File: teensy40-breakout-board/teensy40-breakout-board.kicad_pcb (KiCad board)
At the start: 2 copper layers, 18 x 56.1 mm, 3 parts, among them J1 Conn_01x08, J2 Conn_01x08, U1 Teensy4.0_WithBottomAndEdge

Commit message: Complete routing
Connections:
- net Net-(J1-Pad6) renamed VCC
- net Net-(J1-Pad7) renamed +3V3
- net Net-(J1-Pad8) renamed GND
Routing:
- net Net-(J2-Pad5): track 0.00 -> 28.3 mm, vias 0 -> 1
- net Net-(J2-Pad4): track 0.00 -> 23.4 mm, vias 0 -> 1
- net +3V3: track 0.00 -> 21.2 mm
- net Net-(J2-Pad7): track 0.00 -> 19.9 mm
- net VCC: track 0.00 -> 17.0 mm
- net Net-(J2-Pad6): track 0.00 -> 16.3 mm
- net Net-(J2-Pad3): track 19.9 -> 18.4 mm
- net Net-(J1-Pad5): track 26.1 -> 24.7 mm
- added copper zone on B.Cu, net GND
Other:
- net class Default: clearance 0.2 -> 0.254; trace_width 0.25 -> 0.254; via_dia 0.8 -> 0.762; via_drill 0.4 -> 0.381
- net class Power added: clearance 0.254, trace_width 1.27, via_dia 1.524, via_drill 0.762
- rule trace_clearance: 0.2 -> 0.254

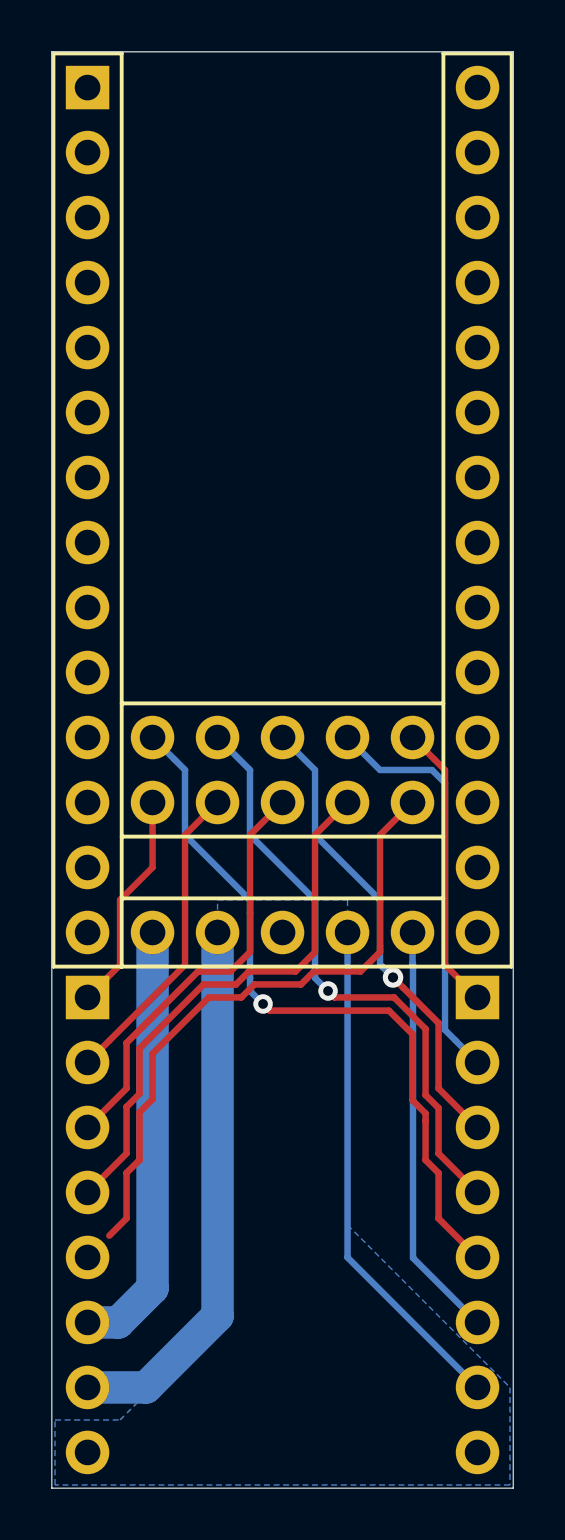
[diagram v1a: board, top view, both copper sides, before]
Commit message: Add top silkscreen labels
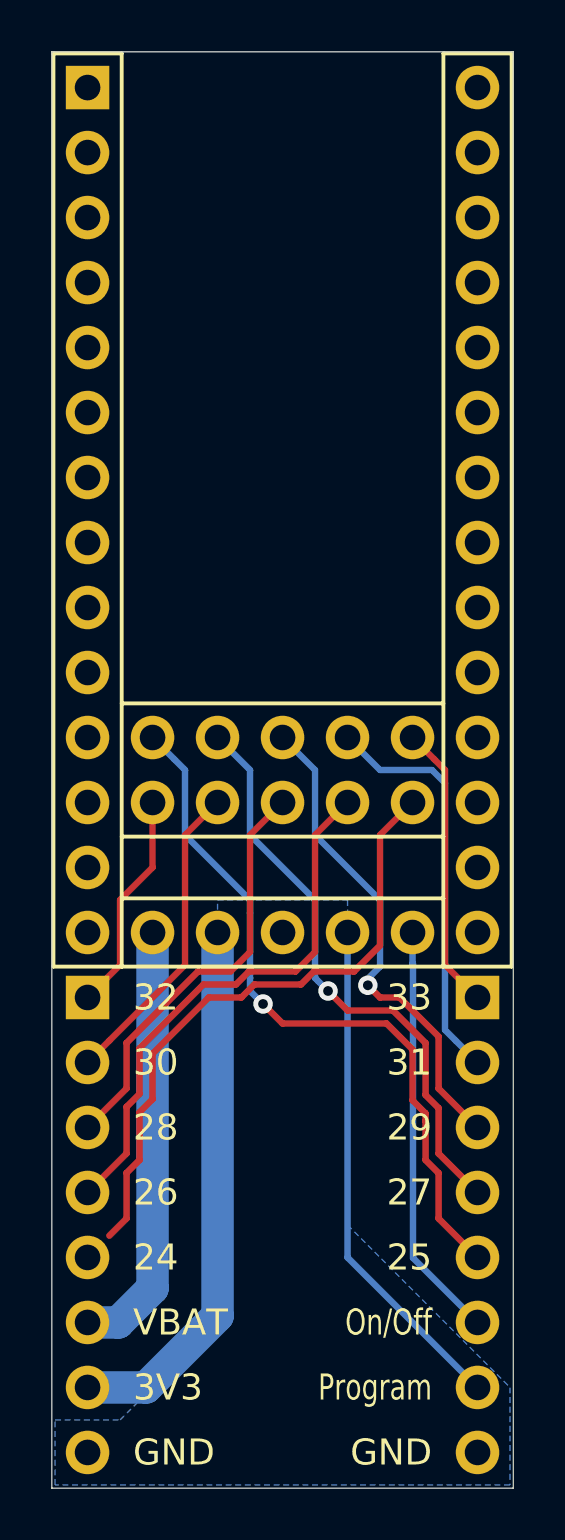
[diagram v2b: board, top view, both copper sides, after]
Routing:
- net Net-(J2-Pad3): track 18.4 -> 19.3 mm
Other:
- board text added: "24"
- board text added: "25"
- board text added: "26"
- board text added: "27"
- board text added: "28"
- board text added: "29"
- board text added: "30"
- board text added: "31"
- board text added: "32"
- board text added: "33"
- board text added: "3V3"
- board text added: "GND"
- board text added: "On/Off"
- board text added: "Program"
- board text added: "VBAT"

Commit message: Label all breakout pins
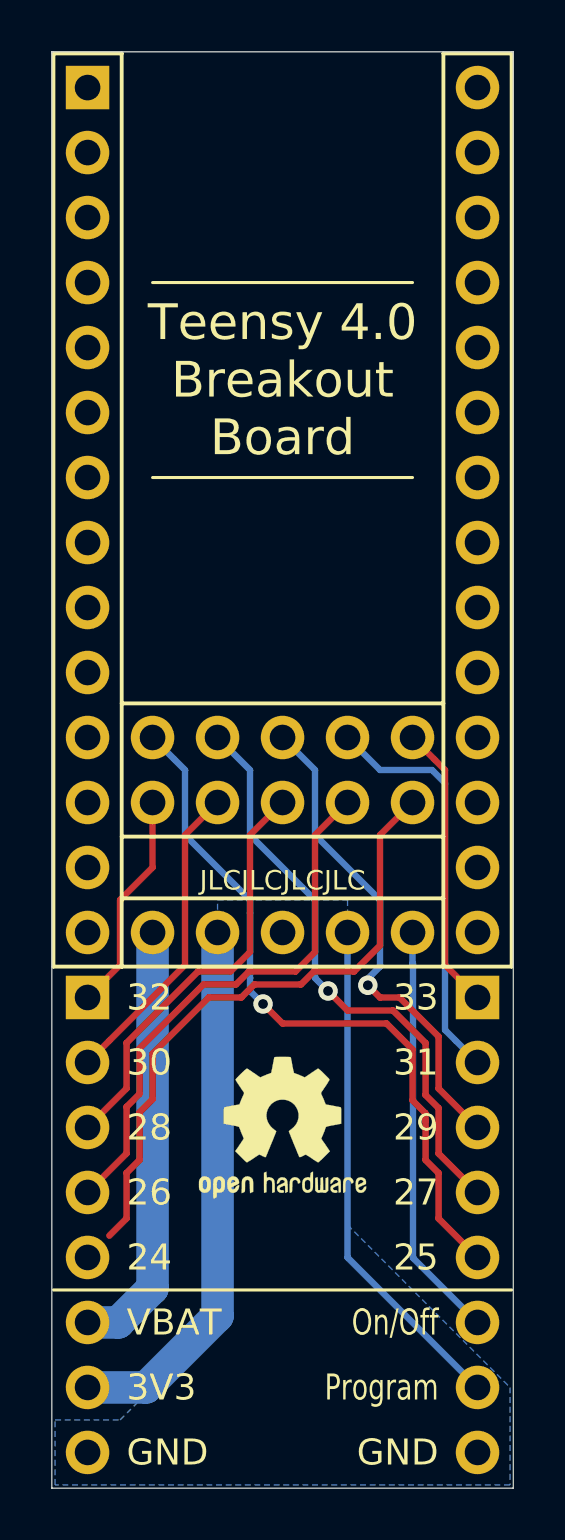
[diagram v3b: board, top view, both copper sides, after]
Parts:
- added REF**: OSHW-Logo2_7.3x6mm_SilkScreen, Symbol:OSHW-Logo2_7.3x6mm_SilkScreen, F.Cu at (134.6, 116.8)
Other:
- board text added: "0"
- board text added: "1"
- board text added: "10"
- board text added: "11"
- board text added: "12"
- board text added: "13"
- board text added: "14"
- board text added: "15"
- board text added: "16"
- board text added: "17"
- board text added: "18"
- board text added: "19"
- board text added: "2"
- board text added: "20"
- board text added: "21"
- board text added: "22"
- board text added: "23"
- board text added: "3"
- board text added: "4"
- board text added: "5"
- board text added: "6"
- board text added: "7"
- board text added: "8"
- board text added: "9"
- board text added: "JLCJLCJLCJLC"
- board text added: "Teensy 4.0 Breakout Board"
- board text added: "VIN"
